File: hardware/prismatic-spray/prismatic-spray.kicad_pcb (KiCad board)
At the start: 2 copper layers, 65 x 115 mm, 10 parts, among them J1 Conn_01x03_Male, J2 Conn_01x03_Male, SW1 SW_Push, SW2 SW_Push, SW3 SW_Push, U1 Pico

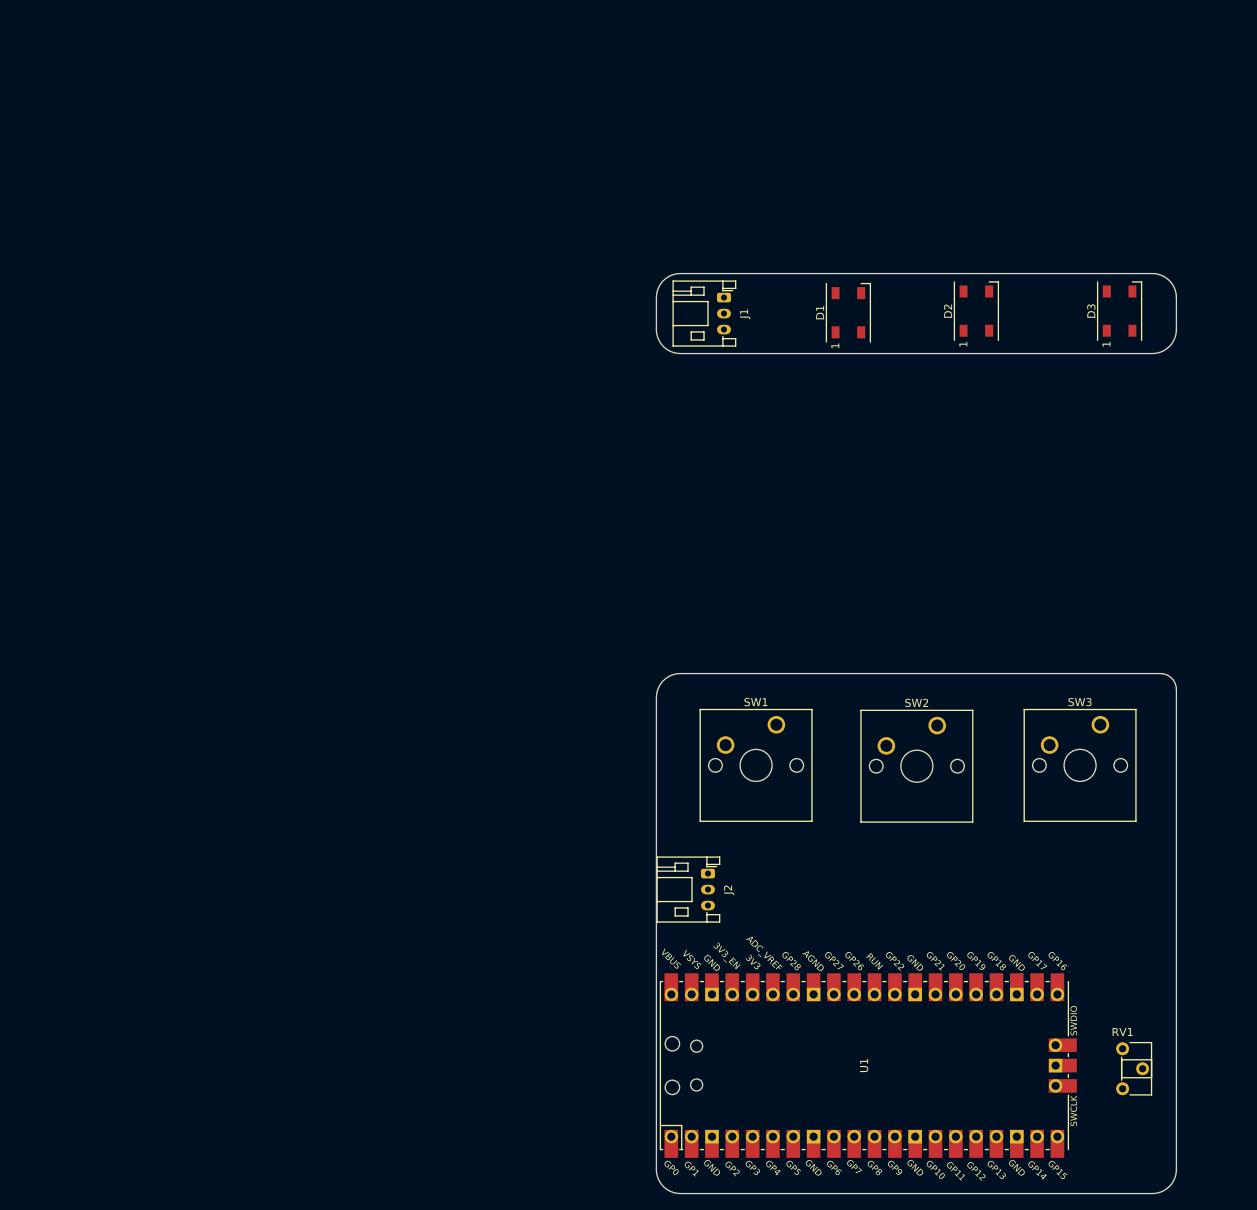
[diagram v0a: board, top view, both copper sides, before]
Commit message: Add mounting holes
- Add non-plated mounting holes
- Reposition board
- Place potentiometer
- TODO: rotary encoder
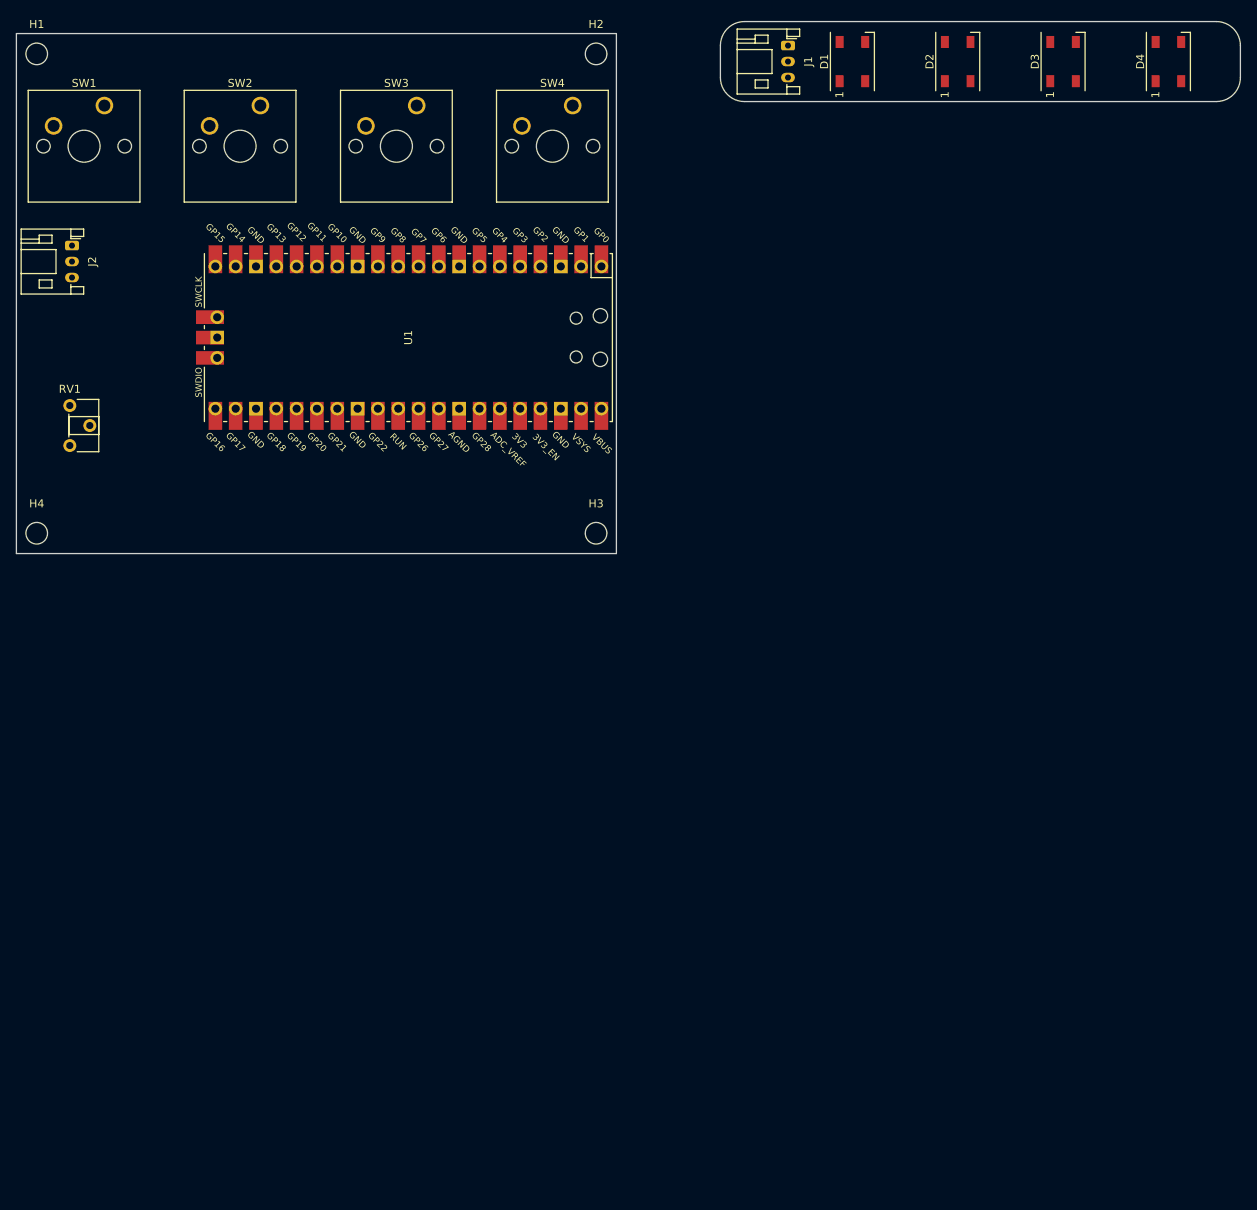
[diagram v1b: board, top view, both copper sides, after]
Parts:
- added D4: WS2812B, LED_SMD:LED_WS2812B_PLCC4_5.0x5.0mm_P3.2mm, F.Cu at (164.0, 23.5)
- added H1: MountingHole, MountingHole:MountingHole_2.7mm_M2.5, F.Cu at (22.5, 22.5)
- added H2: MountingHole, MountingHole:MountingHole_2.7mm_M2.5, F.Cu at (92.5, 22.5)
- added H3: MountingHole, MountingHole:MountingHole_2.7mm_M2.5, F.Cu at (92.5, 82.5)
- added H4: MountingHole, MountingHole:MountingHole_2.7mm_M2.5, F.Cu at (22.5, 82.5)
- added SW4: SW_Push, Button_Switch_Keyboard:SW_Cherry_MX_1.00u_PCB, F.Cu at (89.5, 29.0)
- moved RV1 154.2 mm to (26.7, 66.5)
- moved SW3 115.3 mm to (70.0, 29.0)
- moved SW2 114.7 mm to (50.5, 29.0)
- moved SW1 114.2 mm to (31.0, 29.0)
- moved J2 111.7 mm to (26.9, 46.5)
- moved U1 107.4 mm to (69.0, 58.0), turned to -90 degrees
- moved J1 32.5 mm to (116.5, 21.5)
- moved D3 32.0 mm to (150.8, 23.5)
- moved D1 31.4 mm to (124.5, 23.5)
- moved D2 31.3 mm to (137.7, 23.5)
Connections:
- D3 pad 2: unconnected-(D3-Pad2) -> Net-(D3-Pad2)
- U1 pad 14: Net-(SW3-Pad1) -> Net-(SW4-Pad1)
- U1 pad 15: Net-(SW2-Pad1) -> Net-(SW3-Pad1)
- U1 pad 16: Net-(SW1-Pad1) -> Net-(SW2-Pad1)
- U1 pad 17: unconnected-(U1-Pad17) -> Net-(SW1-Pad1)
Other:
- board size 65 x 115 mm -> 153 x 66.5 mm

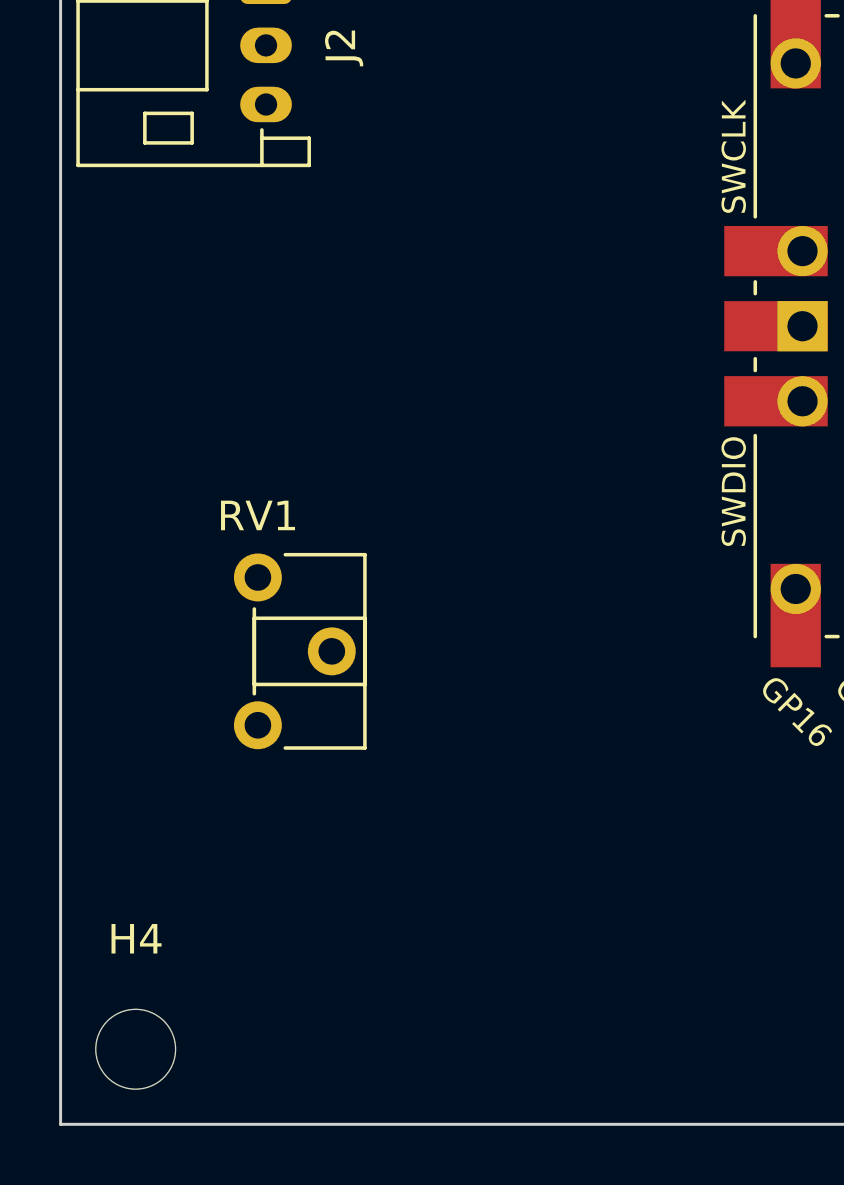
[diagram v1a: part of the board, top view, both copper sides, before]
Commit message: Populate board with more footprints/3d models
- Add Cherry MX key switch 3d model
- Add PEC11 rotary encoder 3d model
- Add Raspberry Pi Pico 3d model
- Add PEC11 footprint (from schematic)
- Change rotary encoder schematic symbol to 3 encoder pins + 2 switch pins
- Add PCB rendering for docs
- Add image to local directory
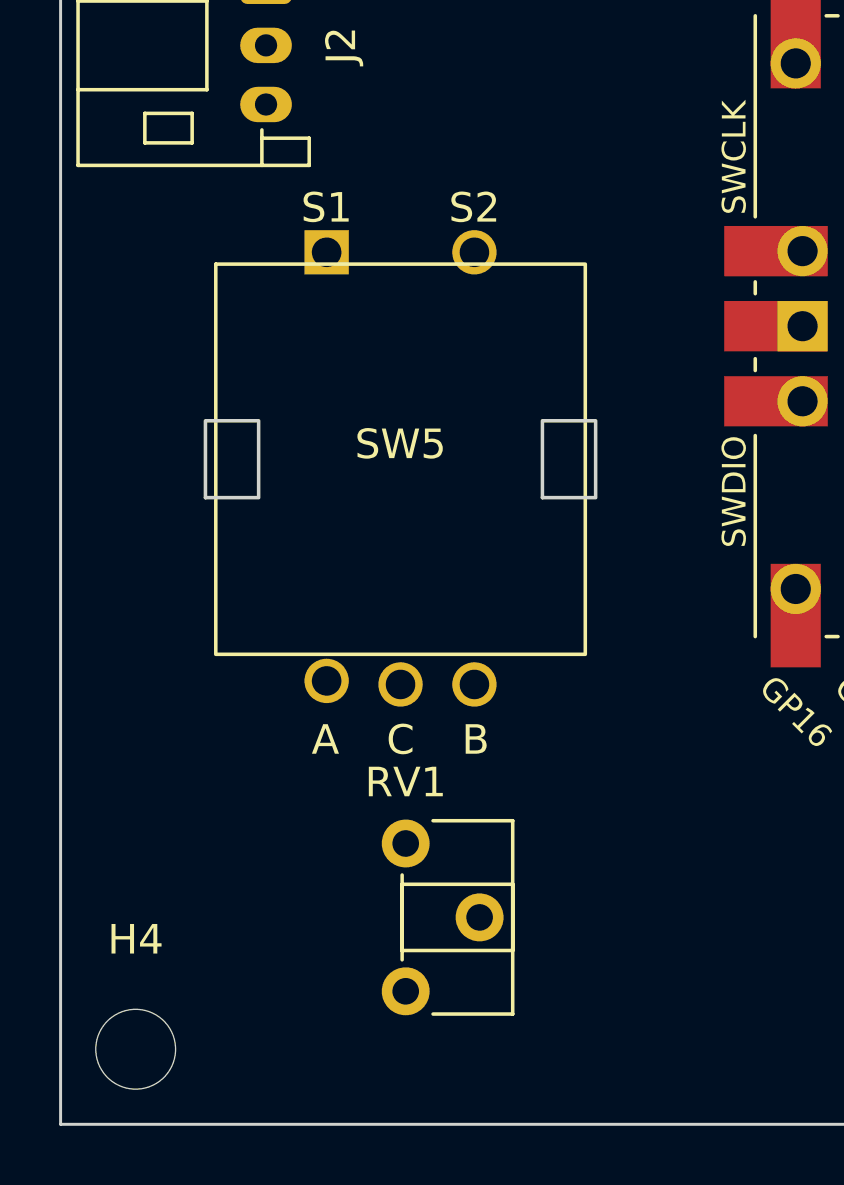
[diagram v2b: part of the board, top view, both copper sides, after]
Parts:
- added SW5: RotaryEncoder_Switch, Footprints:pec11_rotary_encoder, F.Cu at (31.5, 62.5)
- moved RV1 10.3 mm to (31.7, 75.5)
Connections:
- SW4 pad 2: unconnected-(SW4-Pad2) -> +3V3
- U1 pad 4: unconnected-(U1-Pad4) -> Net-(U1-Pad4)
- U1 pad 5: unconnected-(U1-Pad5) -> Net-(U1-Pad5)
- U1 pad 6: unconnected-(U1-Pad6) -> Net-(U1-Pad6)
- U1 pad 7: unconnected-(U1-Pad7) -> Net-(U1-Pad7)

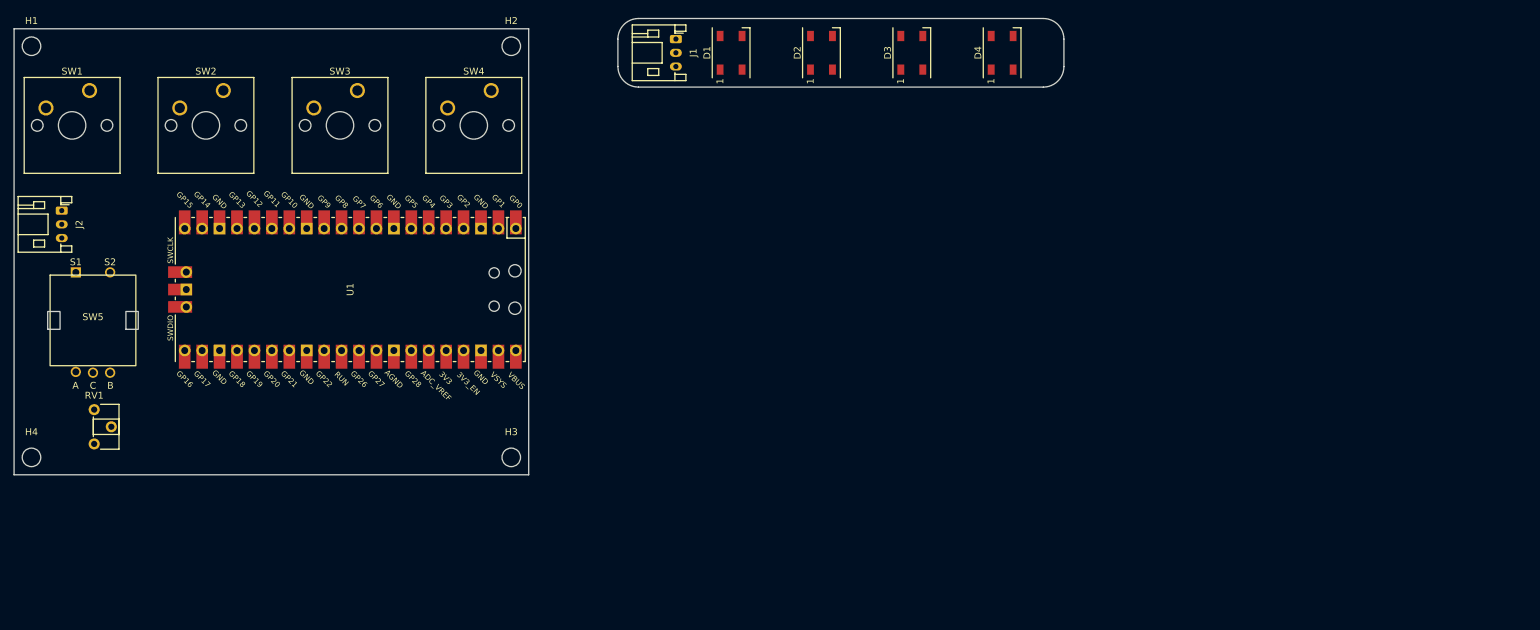
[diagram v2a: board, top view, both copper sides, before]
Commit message: Add P160 Potentiometer
- Add custom footprint
- TODO: add outline/screenprint for PCB size
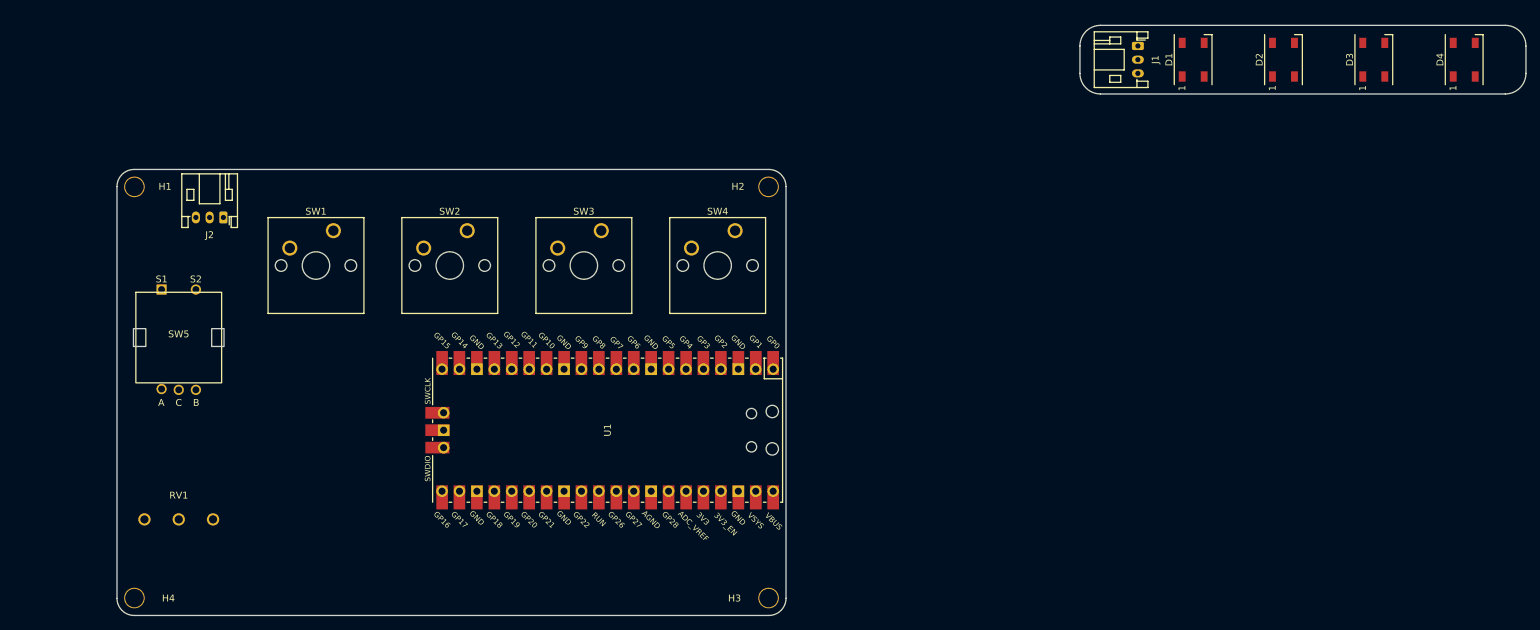
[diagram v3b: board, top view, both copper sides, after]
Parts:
- RV1: footprint Potentiometer_THT:Potentiometer_ACP_CA6-H2,5_Horizontal -> Footprints:p160_potentiometer
- moved D1 67.3 mm to (191.8, 24.5)
- moved D2 67.3 mm to (205.0, 24.5)
- moved D4 67.3 mm to (231.3, 24.5)
- moved J1 67.3 mm to (183.8, 22.5)
- moved D3 67.3 mm to (218.2, 24.5)
- moved H2 42.7 mm to (130.0, 43.0)
- moved H3 42.7 mm to (130.0, 103.0)
- moved U1 42.7 mm to (106.5, 78.5)
- moved SW1 41.0 mm to (66.5, 49.4)
- moved SW2 41.0 mm to (86.0, 49.4)
- moved SW3 41.0 mm to (105.6, 49.4)
- moved SW4 41.0 mm to (125.1, 49.4)
- moved H1 25.4 mm to (37.5, 43.0)
- moved H4 25.4 mm to (37.5, 103.0)
- moved J2 23.6 mm to (50.5, 47.5), turned to 180 degrees
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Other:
- board size 153 x 66.5 mm -> 205.3 x 86 mm
